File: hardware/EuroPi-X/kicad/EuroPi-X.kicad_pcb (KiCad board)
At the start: 2 copper layers, 102.9 x 109.2 mm, 165 parts, among them J1 Conn_01x16_Pin, J10 Thonkiconn_Mono_Jack, J11 Conn_02x08_Odd_Even, J12 Thonkiconn_Mono_Jack, J13 Thonkiconn_Mono_Jack, J14 Thonkiconn_Mono_Jack, J15 Thonkiconn_Mono_Jack, J16 Thonkiconn_Mono_Jack, J17 Thonkiconn_Mono_Jack, J18 Conn_01x03_Pin, J2 Conn_01x16_Pin, J22 Conn_01x11_Pin, J3 Thonkiconn_Mono_Jack, J4 Thonkiconn_Mono_Jack, J5 Conn_01x16_Pin, J6 Thonkiconn_Mono_Jack, J7 Thonkiconn_Mono_Jack, J8 Conn_01x16_Pin, J9 Thonkiconn_Mono_Jack, P1 USB_C_Plug_USB2.0, P2 Potentiometer_9mm_Vertical_Li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, P3 Potentiometer_9mm_Vertical_Li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, Q1 BSS138, SW1 B1, SW2 B2, U1 MCP6002-xSN, U10 MCP3428, U11 L7805, U12 LM4040DBZ-4.1, U2 LM4040DBZ-2.0, U3 LM4040DBZ-10, U4 RP2040, U7 TL074, U8 TL074, U9 MCP6004, Y1 Crystal_GND2

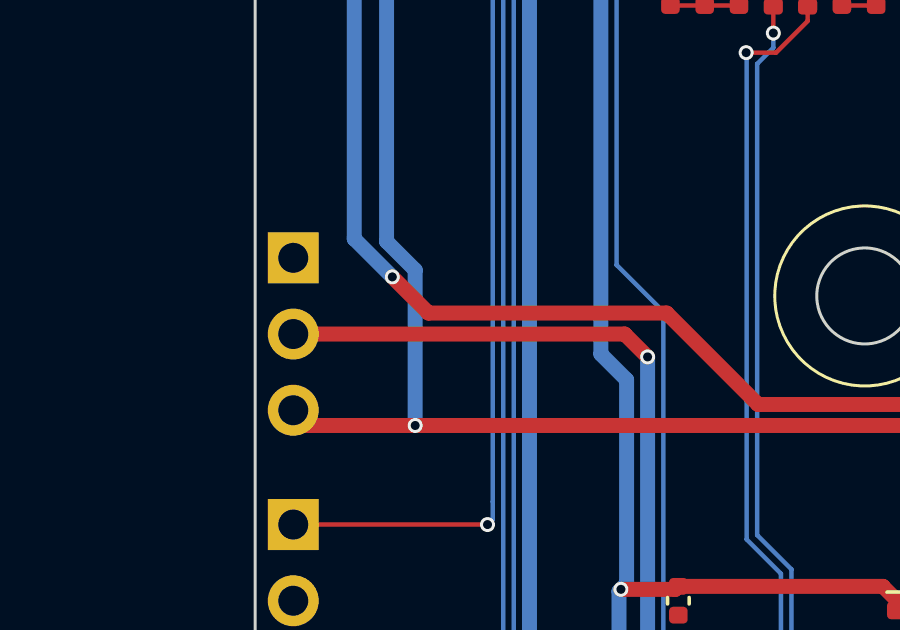
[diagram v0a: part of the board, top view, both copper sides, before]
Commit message: make breadboard compatible
also adjust thermal spoke count in design rules to remove errors (only 1 spoke required)
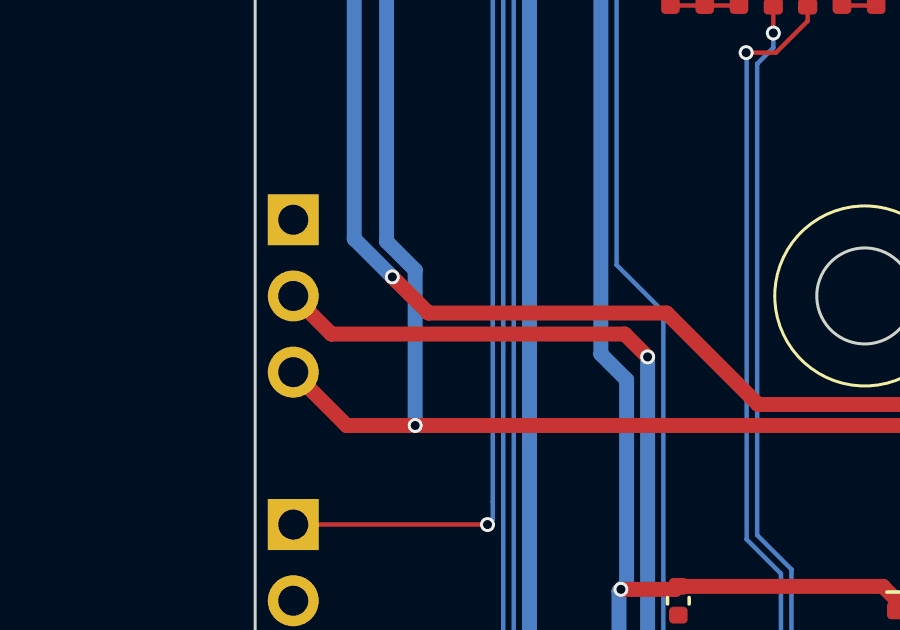
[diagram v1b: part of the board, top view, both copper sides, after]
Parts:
- moved J18 1.27 mm to (63.5, 49.5)
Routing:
- net /5VREG_INPUT: track 31.2 -> 31.8 mm
- net +12V: track 181.7 -> 182.2 mm
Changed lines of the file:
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@@
   )
   (footprint "Connector_PinHeader_2.54mm:PinHeader_1x03_P2.54mm_Vertical" (layer "B.Cu")
-    (at 63.5 50.8 180)
+    (at 63.5 49.53 180)
     (descr "Through hole straight pin header, 1x03, 2.54mm pitch, single row")
     (tags "Through hole pin header THT 1x03 2.54mm single row")
@@
     (effects (font (size 1 1) (thickness 0.15)) (justify bottom))
   )
-  (gr_text "5V REG\nSETTING" (at 60.96 53.34) (layer "User.4")
+  (gr_text "5V REG\nSETTING" (at 60.96 52.07) (layer "User.4")
     (effects (font (size 1 1) (thickness 0.15)) (justify right))
   )
@@
   (segment (start 90.486 41.275) (end 90.484 41.277) (width 0.5) (layer "F.Cu") (net 33))
   (segment (start 88.4585 14.732) (end 86.933 14.732) (width 0.5) (layer "F.Cu") (net 33))
+  (segment (start 65.278 56.388) (end 67.564 56.388) (width 0.5) (layer "F.Cu") (net 33))
   (segment (start 65.278 1.27) (end 65.532 1.016) (width 0.5) (layer "F.Cu") (net 33))
-  (segment (start 64.008 56.388) (end 67.564 56.388) (width 0.5) (layer "F.Cu") (net 33))
-  (segment (start 63.5 55.88) (end 64.008 56.388) (width 0.5) (layer "F.Cu") (net 33))
   (segment (start 92.39 68.58) (end 92.39 66.45) (width 1) (layer "F.Cu") (net 33))
   (segment (start 89.3265 49.403) (end 89.216 49.2925) (width 0.5) (layer "F.Cu") (net 33))
@@
   (segment (start 89.154 57.531) (end 89.154 63.214) (width 0.5) (layer "F.Cu") (net 33))
   (segment (start 99.949 50.419) (end 93.472 50.419) (width 0.5) (layer "F.Cu") (net 33))
+  (segment (start 63.5 54.61) (end 65.278 56.388) (width 0.5) (layer "F.Cu") (net 33))
   (segment (start 92.39 66.45) (end 91.44 65.5) (width 1) (layer "F.Cu") (net 33))
   (segment (start 98.171 41.15) (end 98.90895 41.15) (width 0.5) (layer "F.Cu") (net 33))
@@
   (segment (start 78.23 83.625) (end 78.23 79.425) (width 0.5) (layer "B.Cu") (net 155))
   (segment (start 75.311 70.386) (end 75.311 69.596) (width 0.5) (layer "F.Cu") (net 156))
-  (segment (start 74.549 53.34) (end 75.311 54.102) (width 0.5) (layer "F.Cu") (net 156))
   (segment (start 75.311 69.596) (end 75.057 69.342) (width 0.5) (layer "F.Cu") (net 156))
   (segment (start 77.47 68.834) (end 75.565 68.834) (width 0.5) (layer "F.Cu") (net 156))
+  (segment (start 64.77 53.34) (end 74.549 53.34) (width 0.5) (layer "F.Cu") (net 156))
   (segment (start 75.565 68.834) (end 75.057 69.342) (width 0.5) (layer "F.Cu") (net 156))
-  (segment (start 63.5 53.34) (end 74.549 53.34) (width 0.5) (layer "F.Cu") (net 156))
+  (segment (start 63.5 52.07) (end 64.77 53.34) (width 0.5) (layer "F.Cu") (net 156))
+  (segment (start 74.549 53.34) (end 75.311 54.102) (width 0.5) (layer "F.Cu") (net 156))
   (via (at 75.057 69.342) (size 0.5) (drill 0.3) (layers "F.Cu" "B.Cu") (net 156))
   (via (at 75.311 54.102) (size 0.5) (drill 0.3) (layers "F.Cu" "B.Cu") (net 156))

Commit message: save
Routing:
- net Earth: track 101.2 -> 110.0 mm
- net /AGND_FRONT: track 0.00 -> 1.27 mm
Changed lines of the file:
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@@
   (segment (start 96.139 37.272) (end 96.139 38.6255) (width 0.5) (layer "F.Cu") (net 1))
   (segment (start 67.564 9.779) (end 67.026 10.317) (width 0.15) (layer "F.Cu") (net 1))
+  (segment (start 85.75 78.825) (end 85.75 78.08) (width 0.5) (layer "F.Cu") (net 1))
   (segment (start 91.883 3.81) (end 91.756164 3.683164) (width 0.5) (layer "F.Cu") (net 1))
   (segment (start 86.933 6.35) (end 87.923076 6.35) (width 0.5) (layer "F.Cu") (net 1))
@@
   (segment (start 96.021959 32.385) (end 96.328 32.385) (width 0.15) (layer "F.Cu") (net 1))
   (segment (start 72.263 1.877) (end 72.263 2.794) (width 0.15) (layer "F.Cu") (net 1))
+  (segment (start 63.5 11.43) (end 63.5 8.89) (width 1) (layer "F.Cu") (net 1))
   (segment (start 64.389 8.001) (end 67.437 8.001) (width 0.5) (layer "F.Cu") (net 1))
   (segment (start 88.375819 6.802743) (end 90.352257 6.802743) (width 0.5) (layer "F.Cu") (net 1))
@@
   (segment (start 84.169614 15.492) (end 83.594 14.916386) (width 0.5) (layer "F.Cu") (net 1))
   (segment (start 92.807197 33.659343) (end 92.81154 33.655) (width 0.15) (layer "F.Cu") (net 1))
+  (segment (start 101.6 1.27) (end 100.33 1.27) (width 1) (layer "F.Cu") (net 1))
   (segment (start 78.654 5.35) (end 77.359 5.35) (width 0.15) (layer "F.Cu") (net 1))
+  (segment (start 79.35 78.08) (end 78.74 77.47) (width 0.5) (layer "F.Cu") (net 1))
   (segment (start 89.38 36.957) (end 89.535 37.112) (width 0.15) (layer "F.Cu") (net 1))
   (segment (start 77.9175 20.701) (end 77.978 20.6405) (width 0.15) (layer "F.Cu") (net 1))
@@
   (segment (start 91.756164 3.683164) (end 88.9 3.683164) (width 0.5) (layer "F.Cu") (net 1))
   (segment (start 93.555446 6.012101) (end 93.217547 6.35) (width 0.5) (layer "F.Cu") (net 1))
+  (segment (start 63.5 6.35) (end 63.5 8.89) (width 1) (layer "F.Cu") (net 1))
   (segment (start 91.567 36.922) (end 91.317 36.672) (width 0.15) (layer "F.Cu") (net 1))
   (segment (start 88.3245 13.5125) (end 88.274 13.462) (width 0.5) (layer "F.Cu") (net 1))
@@
   (segment (start 90.352257 6.802743) (end 90.805 6.35) (width 0.5) (layer "F.Cu") (net 1))
   (segment (start 92.807197 33.659343) (end 92.802854 33.655) (width 0.15) (layer "F.Cu") (net 1))
+  (segment (start 85.75 78.08) (end 86.36 77.47) (width 0.5) (layer "F.Cu") (net 1))
   (segment (start 88.536 33.7) (end 88.536 33.691537) (width 0.15) (layer "F.Cu") (net 1))
   (segment (start 83.95 34.16) (end 82.55 35.56) (width 0.15) (layer "F.Cu") (net 1))
@@
   (segment (start 96.789 35.372) (end 97.854 35.372) (width 0.15) (layer "F.Cu") (net 172))
   (segment (start 97.854 35.372) (end 98.298 35.816) (width 0.15) (layer "F.Cu") (net 172))
+  (segment (start 1.27 11.43) (end 2.54 11.43) (width 1) (layer "F.Cu") (net 175))
   (zone (net 87) (net_name "/GND_FRONT") (layers "F&B.Cu") (hatch edge 0.5)
     (connect_pads (clearance 0.5))

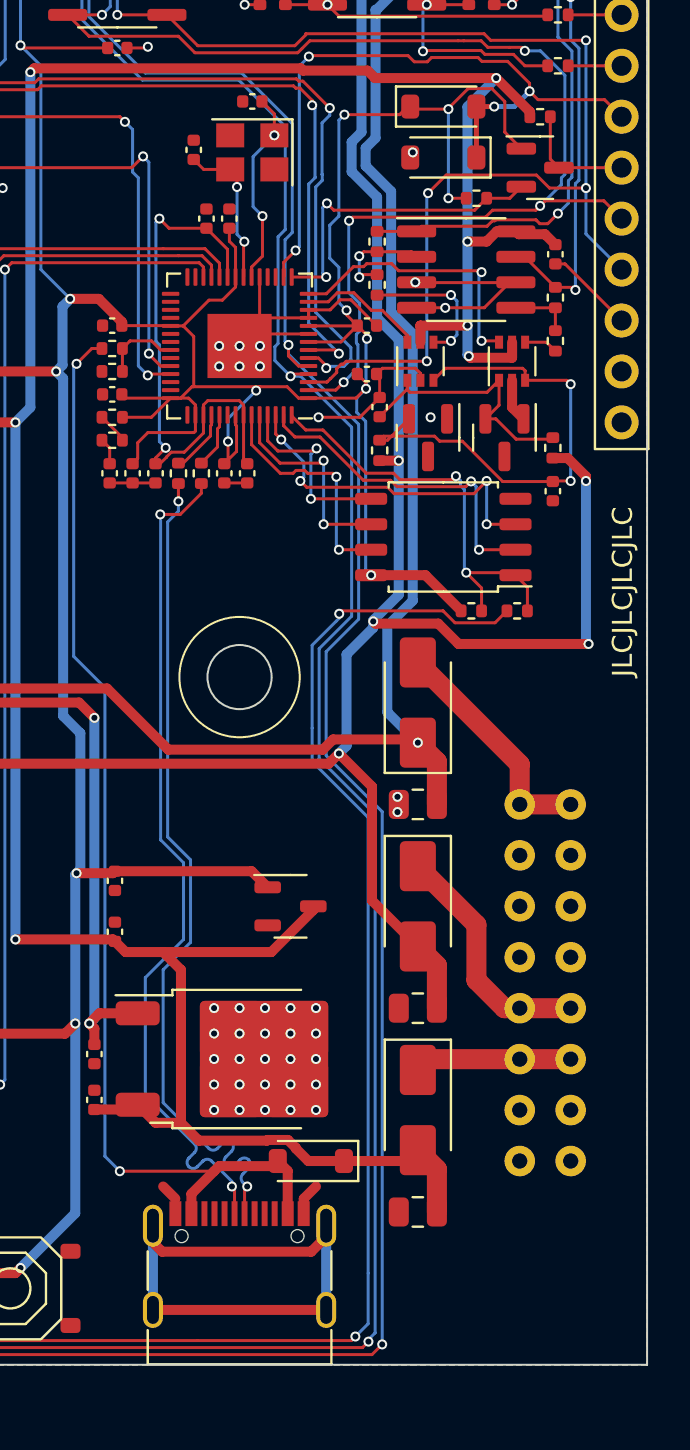
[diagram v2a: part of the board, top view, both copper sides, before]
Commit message: add led to pcb
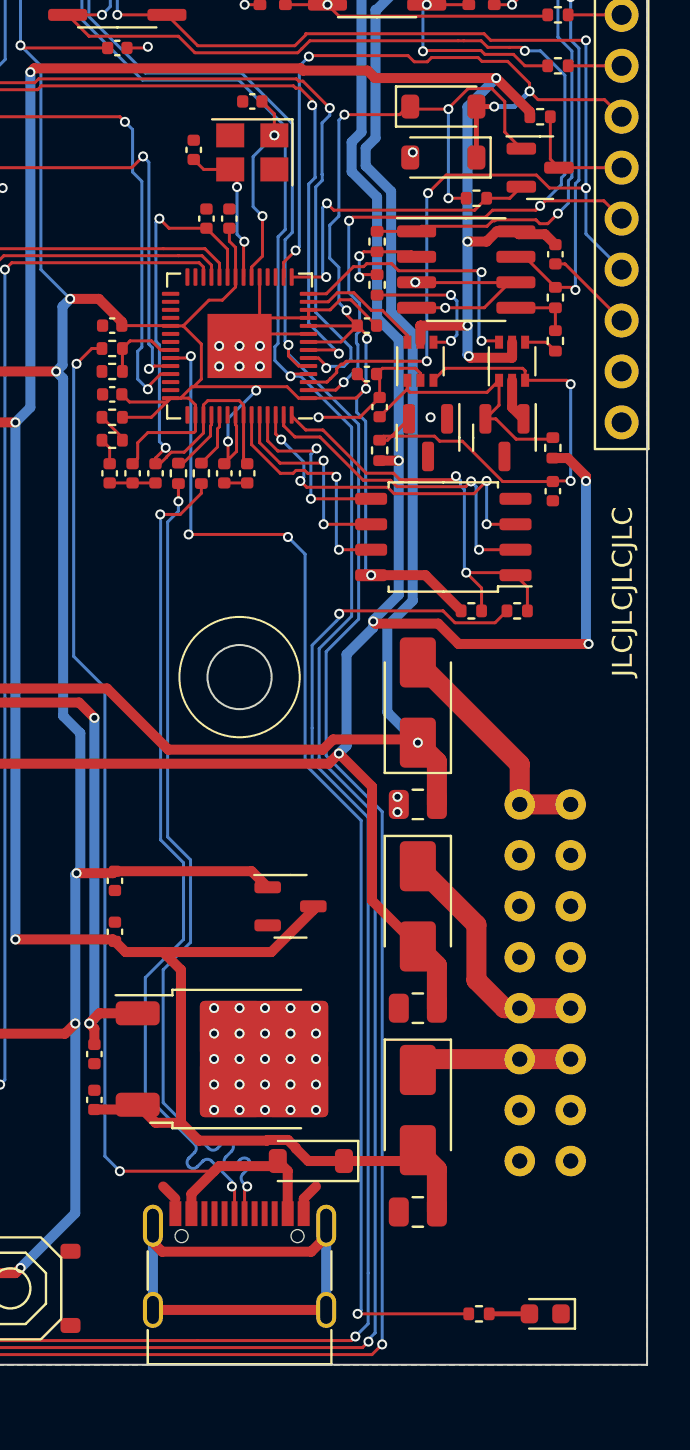
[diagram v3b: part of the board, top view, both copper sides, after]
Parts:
- added D7: LED, LED_SMD:LED_0603_1608Metric, F.Cu at (97.8, 83.8)
- added R62: 200R, Resistor_SMD:R_0402_1005Metric, F.Cu at (94.5, 83.8)
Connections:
- U4 pad 37: unconnected-(U4-GPIO25-Pad37) -> /GPIO_25_LED
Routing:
- net /GPIO_25_LED: track 0.00 -> 60.8 mm, vias 0 -> 4
- net Net-(D7-A): track 0.00 -> 2.00 mm
- net /KNOB_2: track 27.7 -> 28.9 mm
- net /KNOB_1: track 25.8 -> 26.5 mm
